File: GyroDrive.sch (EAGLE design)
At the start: 53 parts, among them U2 2.5V, U3 ANALOG-DEVICES-E14_AD8426ACPZ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, U4 ANALOG-DEVICES-E14_AD8426ACPZ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, X1 OMN-A75243-001

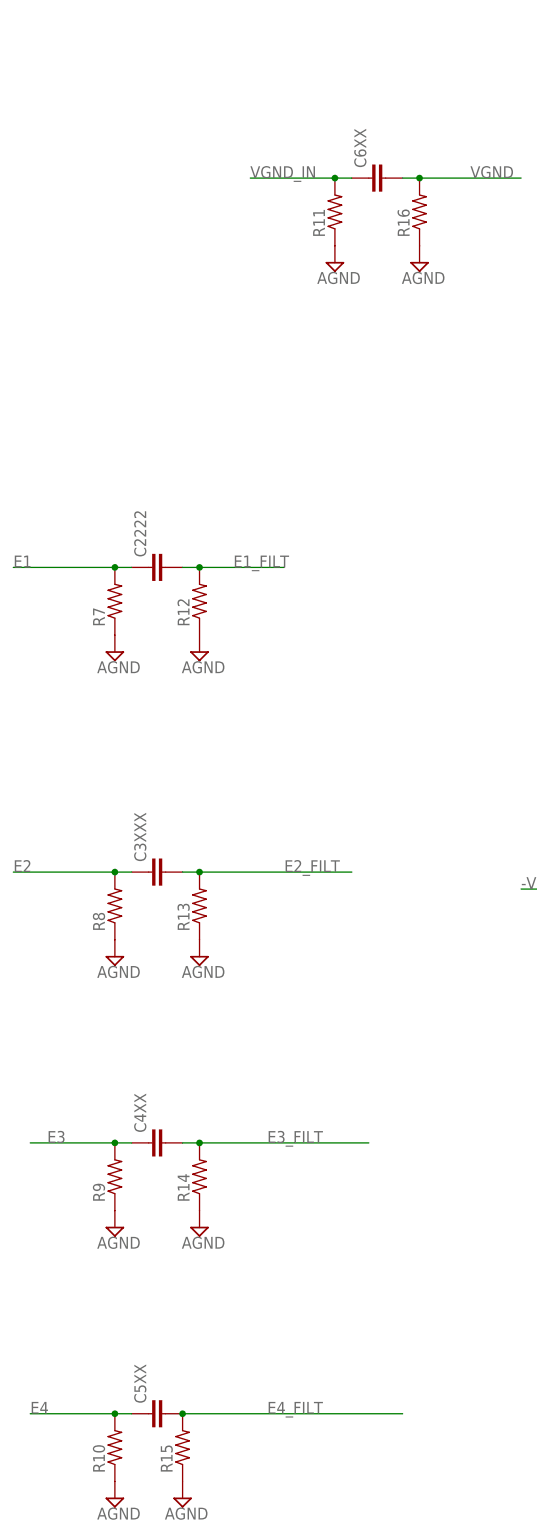
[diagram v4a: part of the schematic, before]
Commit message: Removed resistor to ground before blocking capacitors
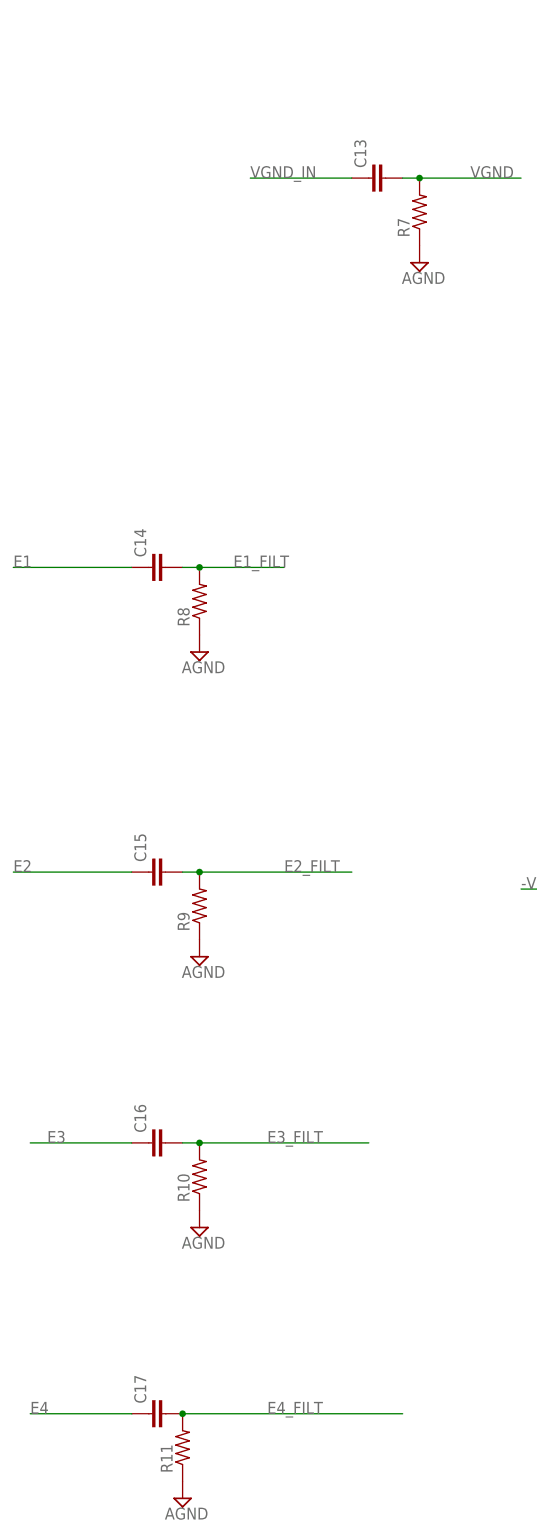
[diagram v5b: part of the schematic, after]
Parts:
- removed R12, R13, R14, R15, R16: (no value), resistor:R-US_R0201
- renumbered C2222 to C14, C3XXX to C15, C4XX to C16, C5XX to C17, C6XX to C13
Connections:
- net AGND: no longer R12.1, R13.1, R14.1, R15.1, R16.1
- net E1: no longer R7.2
- net E1_FILT: now also R8.2; no longer R12.2
- net E2: no longer R8.2
- net E2_FILT: now also R9.2; no longer R13.2
- net E3: no longer R9.2
- net E3_FILT: now also R10.2; no longer R14.2
- net E4: no longer R10.2
- net E4_FILT: now also R11.2; no longer R15.2
- net VGND: now also R7.2; no longer R16.2
- net VGND_IN: no longer R11.2
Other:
- moved on the sheet: R10, R11, R7, R8, R9

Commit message: analog schematic for thesis
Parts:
- removed C1, C2: 0.1uF, resistor:C-EUC0402
- removed C3: 10nF, resistor:C-EUC0402
- removed C4: 10uF, resistor:C-EUC0603
- removed C5, C6: (no value), resistor:C-EUC0402
- removed J_SCL, J_SDA: (no value), michael-stetner:SJ
- removed R1, R2: 10k, resistor:R-US_R0201
- removed STIMIN, STIMOUT: (no value), michael-stetner:THROUGH-HOLE-30MIL/15MIL
- removed U1: (no value), Grove - IMU 10DOF v1.1:MPU-9250
- removed U2: 2.5V, michael-stetner:TPS715-FIXED
- removed X1: OMN-A75243-001, GFL:OMN-A75243-001
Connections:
- removed net DGND: C1.2, C2.2, C3.2, C4.2, C5.2, C6.2, U1.FSYNC, U1.GND, U1.RESV@2, U2.GND, X1.A
- removed net N$7: C1.1, U1.REGOUT
- removed net SCL: J_SCL.1, R1.1, U1.SCL/SCLK
- removed net SCLOUT: J_SCL.2, X1.E
- removed net SDA: J_SDA.1, R2.1, U1.SDA/SDI
- removed net SDAOUT: J_SDA.2, X1.N
- removed net STIMIN: STIMIN.P, X1.P
- removed net STIMOUT: STIMOUT.P, X1.K
- removed net VDD: C2.1, C3.1, C4.1, C5.1, R1.2, R2.2, U1.AD0/SDO, U1.NCS, U1.RESV, U1.VDD, U1.VDDIO, U2.OUT
- net +VS: no longer C6.1, U2.IN, X1.T
- net -VS: no longer X1.U
- net AGND: no longer X1.D
- net ICOM: no longer X1.B
- net IX: no longer X1.V
- net S1: no longer X1.R
- net S2: no longer X1.L
- net S3: no longer X1.F
- net S4: no longer X1.J
- net VGND_IN: no longer VGND.P
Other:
- note added: "Analog Ground"
- note added: "Bypass capacitors for instrumentation amplifiers"
- note added: "Connect this jumper to use AGND as reference"
- note added: "High-pass filter on electrodes and reference"
- note added: "Instrumentation Amplifiers"
- note added: "Motor and through holes for motor wires"
- note removed: "SMD Solder Jumpers For Debugging"
- note removed: "Voltage Regulator"
